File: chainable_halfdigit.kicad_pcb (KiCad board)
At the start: 2 copper layers, 100 x 100 mm, 48 parts, among them J1 Conn_01x03, J2 Conn_01x03

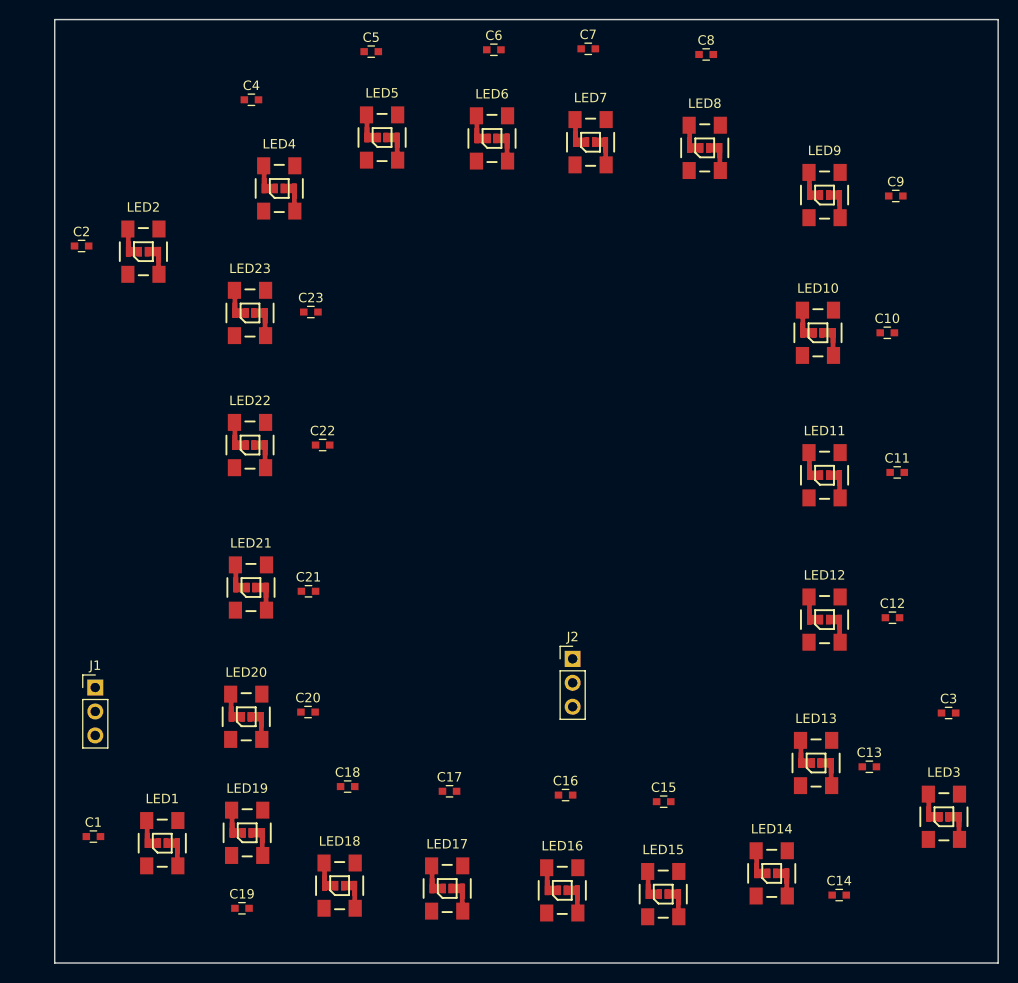
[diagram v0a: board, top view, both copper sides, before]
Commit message: Placed components in PCB
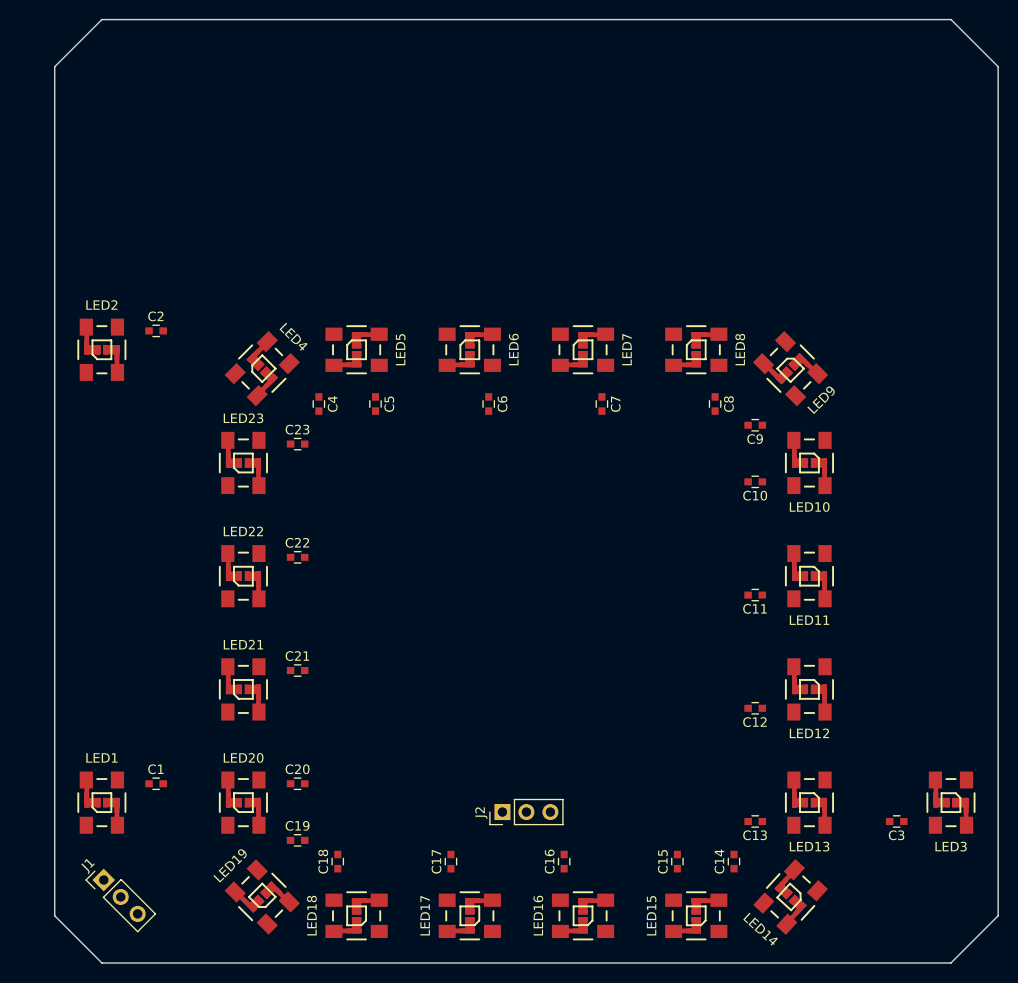
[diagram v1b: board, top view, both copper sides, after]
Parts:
- moved C7 37.7 mm to (148.0, 90.8), turned to 270 degrees
- moved C6 37.6 mm to (136.0, 90.8), turned to 270 degrees
- moved C5 37.4 mm to (124.0, 90.8), turned to 270 degrees
- moved C8 37.1 mm to (160.0, 90.8), turned to 270 degrees
- moved C4 33.0 mm to (118.0, 90.8), turned to 270 degrees
- moved C9 28.5 mm to (164.2, 93.0), turned to 180 degrees
- moved LED5 22.7 mm to (122.0, 85.0), turned to 270 degrees
- moved LED6 22.5 mm to (134.0, 85.0), turned to 270 degrees
- moved LED7 22.0 mm to (146.0, 85.0), turned to 270 degrees
- moved LED8 21.4 mm to (158.0, 85.0), turned to 270 degrees
- moved C10 21.1 mm to (164.2, 99.0), turned to 180 degrees
- moved J1 20.4 mm to (95.2, 141.2), turned to 45 degrees
- moved C11 19.9 mm to (164.2, 111.0), turned to 180 degrees
- moved LED4 19.2 mm to (112.0, 87.0), turned to 315 degrees
- moved LED9 18.7 mm to (168.0, 87.0), turned to 225 degrees
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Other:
- outline, holes or cut-outs redrawn

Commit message: Made pretty lib as local. Added 3D model to leds.
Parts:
- LED1, LED10, LED11, LED12, LED13, LED14, LED15, LED16, LED17, LED18, LED19, LED2, LED20, LED21, LED22, LED23, LED3, LED4, LED5, LED6, LED7, LED8, LED9: footprint WS2812B:WS2812B_data-bridgeable -> lib_fp:WS2812B_data-bridgeable

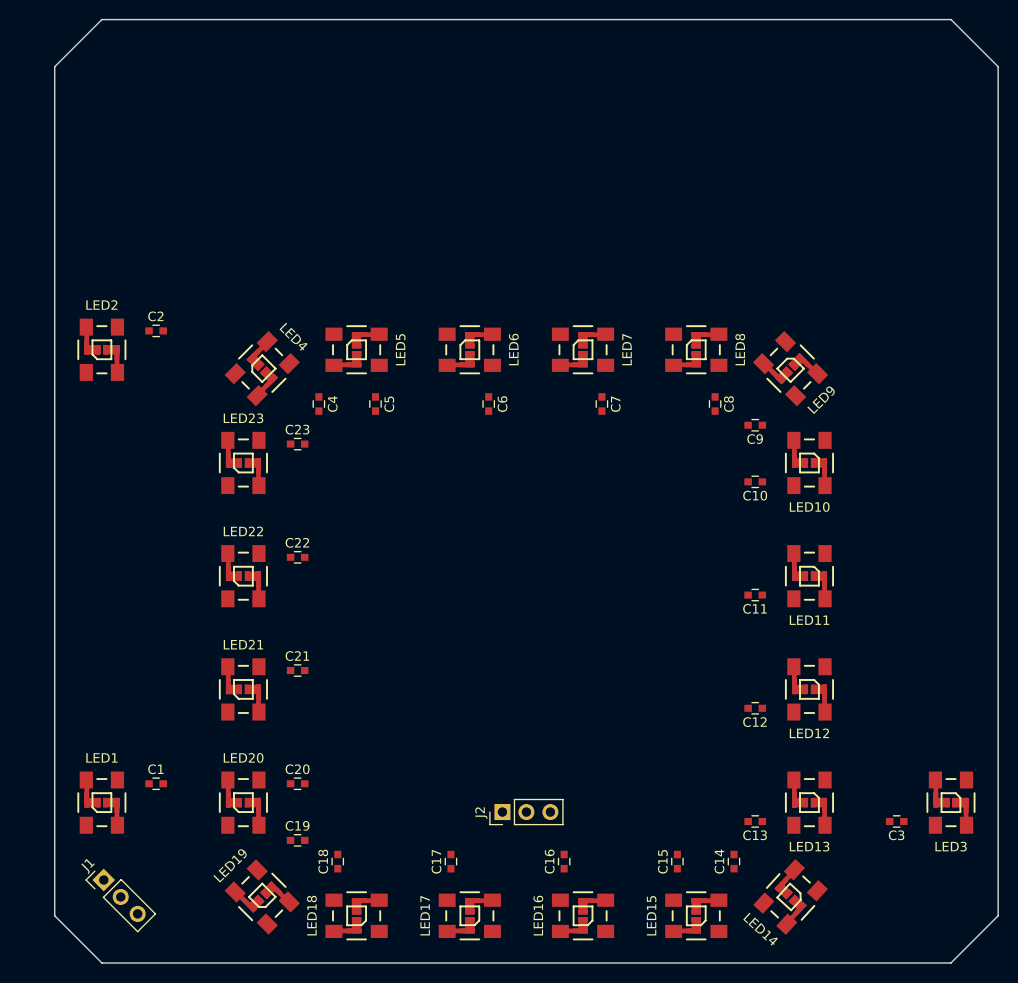
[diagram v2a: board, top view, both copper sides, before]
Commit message: Added tracks
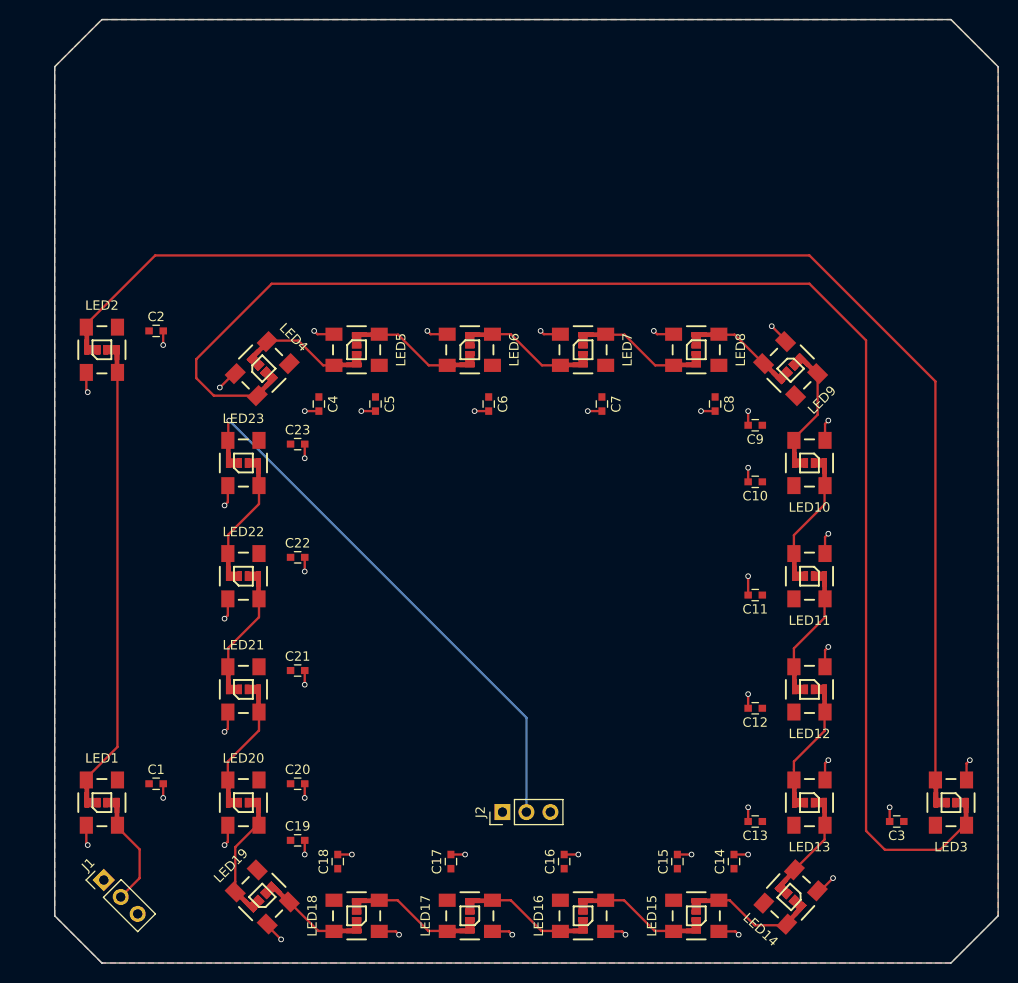
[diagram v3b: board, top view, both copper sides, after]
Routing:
- net Net-(LED3-Pad2): track 0.00 -> 151.9 mm
- net Net-(LED2-Pad2): track 0.00 -> 142.5 mm
- net GND: track 0.00 -> 86.4 mm, vias 0 -> 46
- net DATA_OUT: track 0.00 -> 58.1 mm, vias 0 -> 1
- net Net-(LED1-Pad2): track 0.00 -> 44.6 mm
- net Net-(LED19-Pad2): track 0.00 -> 10.9 mm
- net Net-(LED22-Pad2): track 0.00 -> 10.6 mm
- net Net-(LED21-Pad2): track 0.00 -> 10.6 mm
- net Net-(LED11-Pad2): track 0.00 -> 10.6 mm
- net Net-(LED7-Pad2): track 0.00 -> 9.95 mm
- net Net-(LED5-Pad2): track 0.00 -> 9.95 mm
- net Net-(LED17-Pad2): track 0.00 -> 9.95 mm
- net Net-(LED15-Pad2): track 0.00 -> 9.95 mm
- net Net-(LED12-Pad2): track 0.00 -> 9.95 mm
- net Net-(LED10-Pad2): track 0.00 -> 9.95 mm
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- added copper zone on F.Cu, net 5V
- added copper zone on B.Cu, net GND

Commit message: Edited net sizes
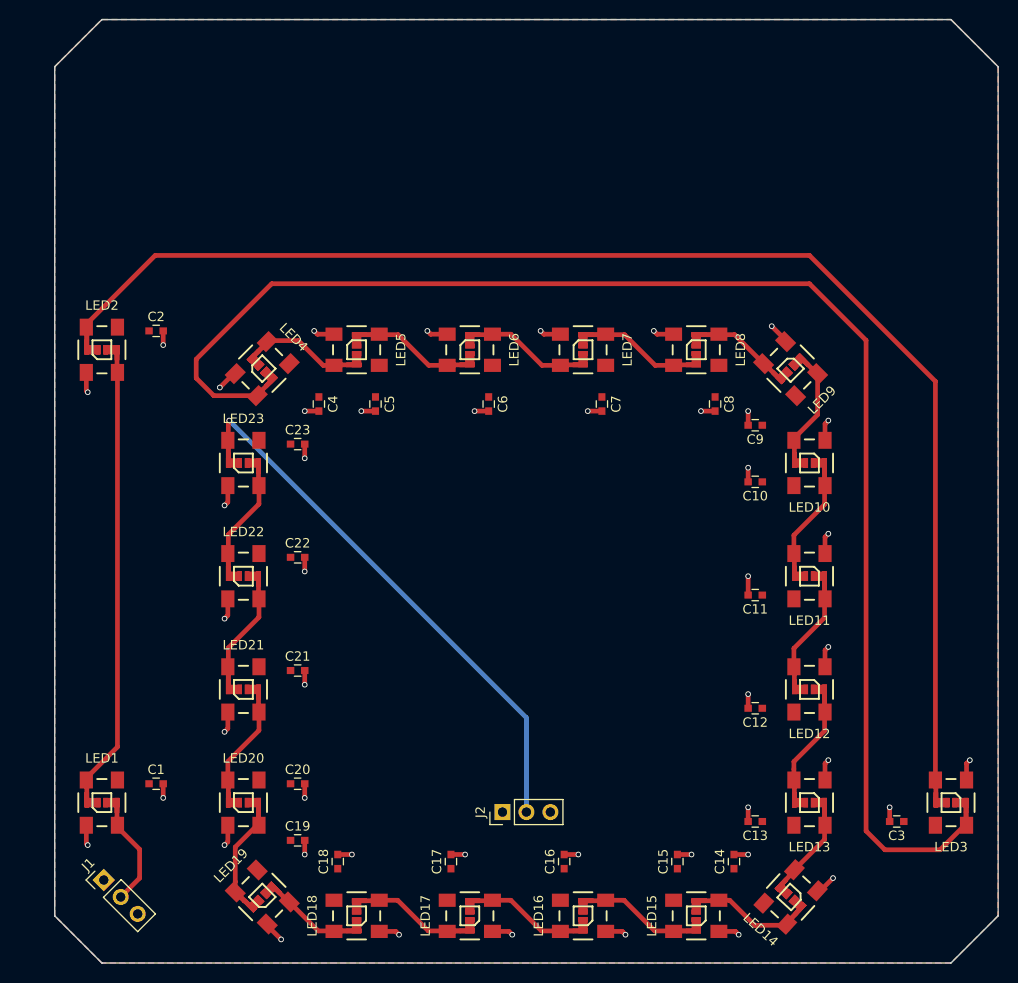
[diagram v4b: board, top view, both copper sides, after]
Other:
- net class DATA added: clearance 0.2, trace_width 0.5, via_dia 0.6, via_drill 0.4
- net class POWER added: clearance 0.2, trace_width 0.5, via_dia 0.6, via_drill 0.4

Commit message: Added instructions on PCB
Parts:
- added G***: LOGO, lib_fp:legend_item_round_circled, F.Cu at (137.4, 130.8)
- added G***: LOGO, lib_fp:legend_item_round_circled, F.Cu at (104.6, 64.6)
- added G***: LOGO, lib_fp:legend_item_round_stripe, F.Cu at (104.6, 62.0)
- added G***: LOGO, lib_fp:legend_item_round_plain, F.Cu at (104.6, 59.4)
- added G***: LOGO, lib_fp:legend_item_round_stripe, F.Cu at (140.0, 130.8)
- added G***: LOGO, lib_fp:legend_item_round_plain, F.Cu at (142.6, 130.8)
- added G***: LOGO, lib_fp:legend_item_round_circled, F.Cu at (96.4, 147.0)
- added G***: LOGO, lib_fp:legend_item_round_stripe, F.Cu at (94.6, 145.2)
- added G***: LOGO, lib_fp:legend_item_round_plain, F.Cu at (92.8, 143.4)
- added G***: LOGO, lib_fp:legend_item_round_circled, F.Cu at (132.6, 67.2)
- added G***: LOGO, lib_fp:legend_item_round_stripe, F.Cu at (132.6, 64.6)
- added G***: LOGO, lib_fp:legend_item_round_plain, F.Cu at (132.6, 62.0)
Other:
- board text added: "In the case you read the text this way: 5V DATA GND"
- board text added: "In the case you read the text this way: 5V DATA GND Turn LEDs 180°"

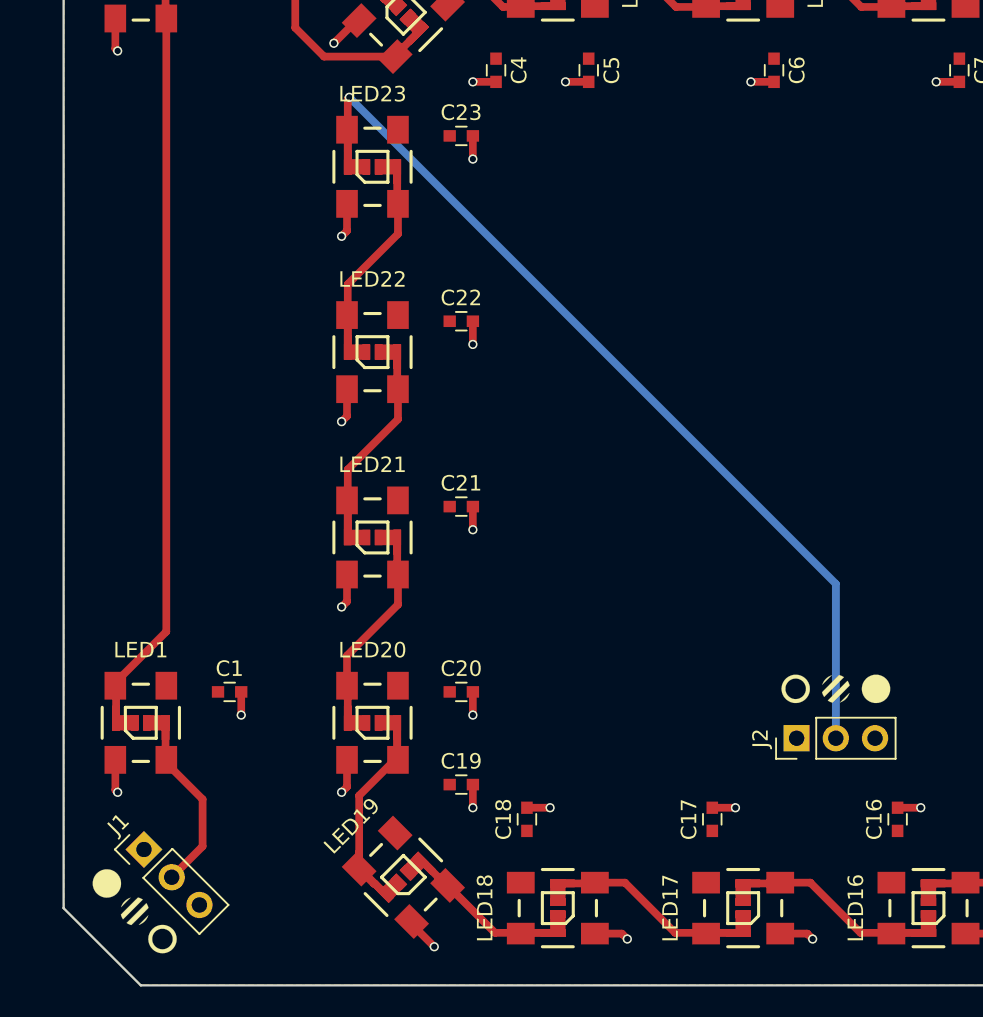
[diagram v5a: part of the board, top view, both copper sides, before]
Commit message: Reverse 5V and DATA to avoid circuit damage when reversing connector.
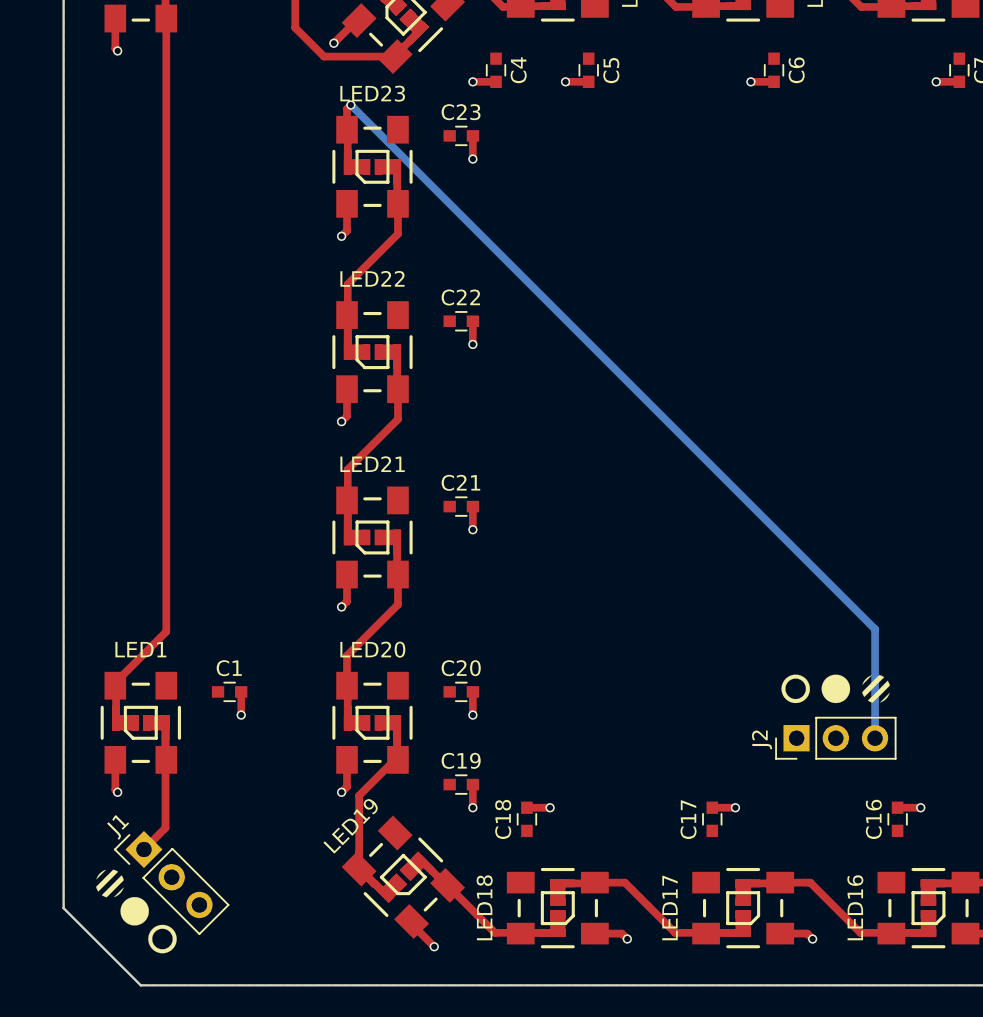
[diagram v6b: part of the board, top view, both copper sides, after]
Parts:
- moved G*** 2.60 mm to (142.6, 130.8)
- moved G*** 2.60 mm to (140.0, 130.8)
- moved G*** 2.55 mm to (94.6, 145.2)
- moved G*** 2.41 mm to (93.0, 143.4)
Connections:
- J1 pad 1: 5V -> DATA_IN
- J1 pad 2: DATA_IN -> 5V
- J2 pad 2: DATA_OUT -> 5V
- J2 pad 3: 5V -> DATA_OUT
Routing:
- net DATA_IN: track 9.40 -> 7.78 mm
- net DATA_OUT: track 58.1 -> 56.8 mm
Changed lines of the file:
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@@
 (kicad_pcb (version 4) (host pcbnew 4.0.7)
   (general
-    (links 0)
-    (no_connects 0)
+    (links 302)
+    (no_connects 2)
     (area 89.924999 49.924999 190.075001 150.075001)
     (thickness 1.6)
     (drawings 10)
-    (tracks 203)
+    (tracks 201)
     (zones 0)
     (modules 60)
@@
   )
   (module lib_fp:legend_item_round_stripe (layer F.Cu)
-    (at 140 130.8)
+    (at 142.6 130.8)
     (fp_text reference G*** (at 0 0) (layer F.SilkS) hide
       (effects (font (thickness 0.3)))
@@
   )
   (module lib_fp:legend_item_round_plain (layer F.Cu)
-    (at 142.6 130.8)
+    (at 140 130.8)
     (fp_text reference G*** (at 0 0) (layer F.SilkS) hide
       (effects (font (thickness 0.3)))
@@
   )
   (module lib_fp:legend_item_round_stripe (layer F.Cu)
-    (at 94.6 145.2)
+    (at 93 143.4)
     (fp_text reference G*** (at 0 0) (layer F.SilkS) hide
       (effects (font (thickness 0.3)))
@@
   )
   (module lib_fp:legend_item_round_plain (layer F.Cu)
-    (at 92.8 143.4)
+    (at 94.6 145.2)
     (fp_text reference G*** (at 0 0) (layer F.SilkS) hide
       (effects (font (thickness 0.3)))
@@
       (net 1 GND))
     (pad 2 thru_hole oval (at 0 2.54 90) (size 1.7 1.7) (drill 1) (layers *.Cu *.Mask)
-      (net 4 DATA_OUT))
-    (pad 3 thru_hole oval (at 0 5.08 90) (size 1.7 1.7) (drill 1) (layers *.Cu *.Mask)
       (net 2 5V))
+    (pad 3 thru_hole oval (at 0 5.08 90) (size 1.7 1.7) (drill 1) (layers *.Cu *.Mask)
+      (net 4 DATA_OUT))
     (model ${KISYS3DMOD}/Pin_Headers.3dshapes/Pin_Header_Straight_1x03_Pitch2.54mm.wrl
       (at (xyz 0 0 0))
@@
     )
     (pad 1 thru_hole rect (at 0 0 45) (size 1.7 1.7) (drill 1) (layers *.Cu *.Mask)
-      (net 2 5V))
-    (pad 2 thru_hole oval (at 0 2.54 45) (size 1.7 1.7) (drill 1) (layers *.Cu *.Mask)
       (net 3 DATA_IN))
+    (pad 2 thru_hole oval (at 0 2.54 45) (size 1.7 1.7) (drill 1) (layers *.Cu *.Mask)
+      (net 2 5V))
     (pad 3 thru_hole oval (at 0 5.08 45) (size 1.7 1.7) (drill 1) (layers *.Cu *.Mask)
       (net 1 GND))
@@
   (segment (start 101.5 83) (end 101.5 84.5) (width 0.5) (layer F.Cu) (net 1))
   (via (at 101.5 84.5) (size 0.6) (drill 0.4) (layers F.Cu B.Cu) (net 1))
-  (segment (start 99 137.95) (end 99 141) (width 0.5) (layer F.Cu) (net 3))
-  (segment (start 99 141) (end 97 143) (width 0.5) (layer F.Cu) (net 3))
-  (segment (start 96.65 135.4) (end 96.65 135.6) (width 0.5) (layer F.Cu) (net 3))
-  (segment (start 96.65 135.6) (end 99 137.95) (width 0.5) (layer F.Cu) (net 3))
-  (segment (start 108.5 92.5) (end 140 124) (width 0.5) (layer B.Cu) (net 4))
-  (segment (start 140 124) (end 140 134) (width 0.5) (layer B.Cu) (net 4))
-  (segment (start 108.4 96) (end 108.4 92.6) (width 0.5) (layer F.Cu) (net 4))
-  (segment (start 108.4 92.6) (end 108.5 92.5) (width 0.5) (layer F.Cu) (net 4))
-  (via (at 108.5 92.5) (size 0.6) (drill 0.4) (layers F.Cu B.Cu) (net 4))
+  (segment (start 96.6 134) (end 96.6 139.807898) (width 0.5) (layer F.Cu) (net 3))
+  (segment (start 96.6 139.807898) (end 95.203949 141.203949) (width 0.5) (layer F.Cu) (net 3))
+  (segment (start 108.6 93) (end 142.54 126.94) (width 0.5) (layer B.Cu) (net 4))
+  (segment (start 142.54 126.94) (end 142.54 134) (width 0.5) (layer B.Cu) (net 4))
+  (segment (start 108.35 94.6) (end 108.35 93.25) (width 0.5) (layer F.Cu) (net 4))
+  (segment (start 108.35 93.25) (end 108.6 93) (width 0.5) (layer F.Cu) (net 4))
+  (via (at 108.6 93) (size 0.6) (drill 0.4) (layers F.Cu B.Cu) (net 4))
   (segment (start 93.35 130.6) (end 93.35 130.4) (width 0.5) (layer F.Cu) (net 5))
   (segment (start 93.35 130.4) (end 96.65 127.1) (width 0.5) (layer F.Cu) (net 5))
